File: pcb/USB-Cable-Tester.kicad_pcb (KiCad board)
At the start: 2 copper layers, 50 x 64 mm, 45 parts, among them J1 USB_C_IN, J2 USB_C_OUT, J3 USB_C_Power

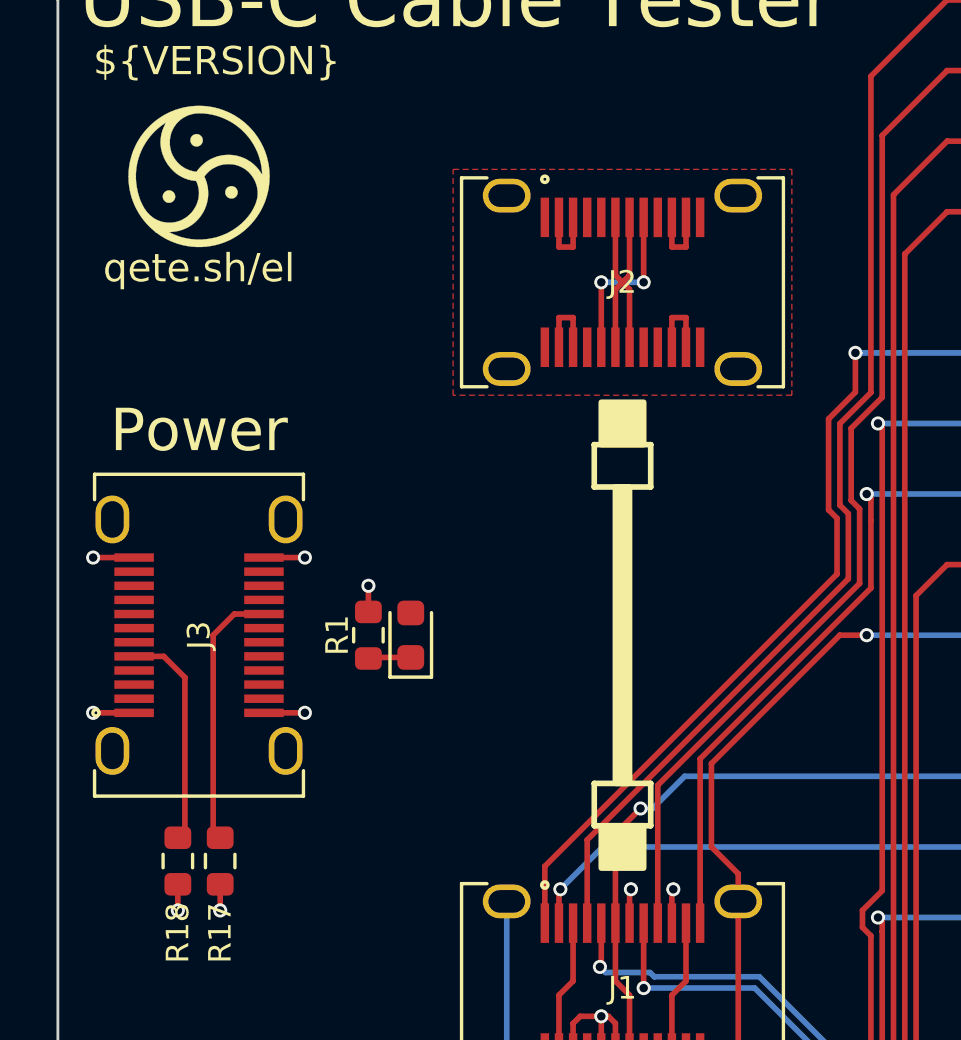
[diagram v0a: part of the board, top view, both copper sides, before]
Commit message: style: silkscreen additions
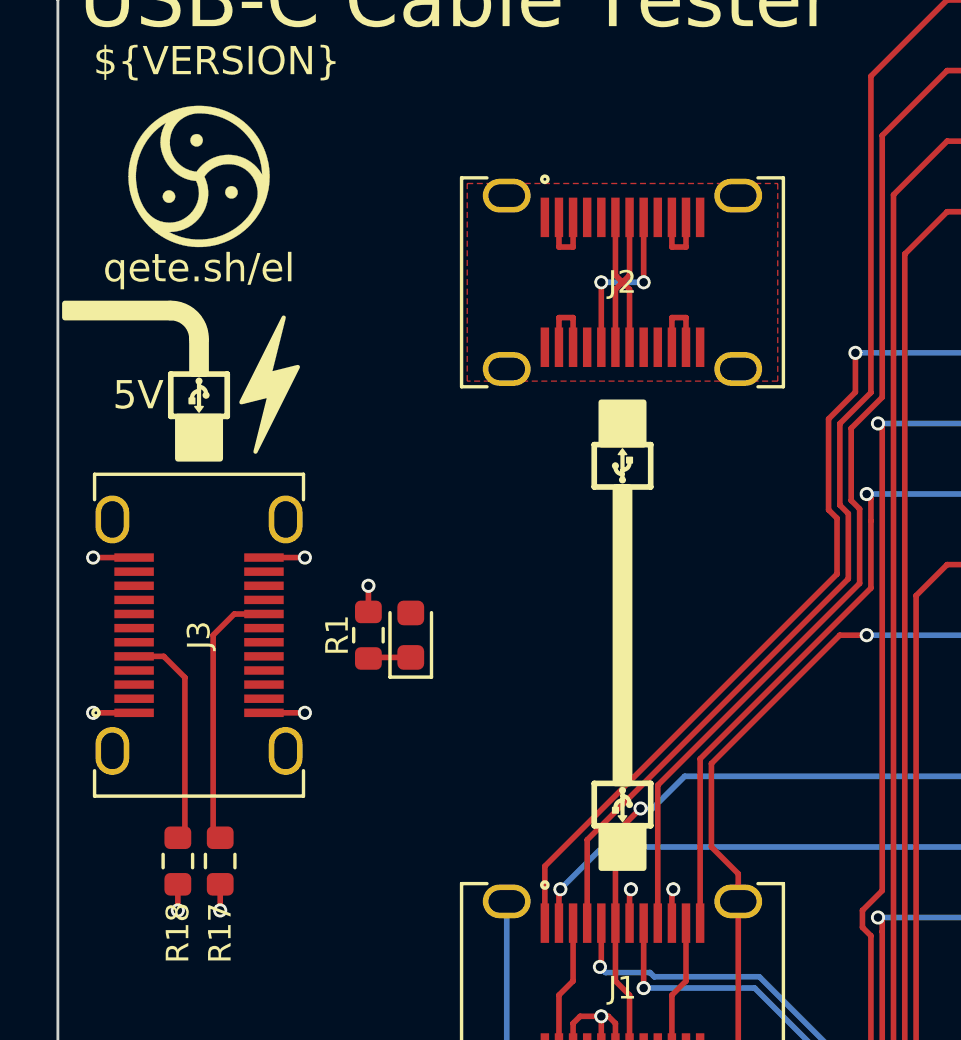
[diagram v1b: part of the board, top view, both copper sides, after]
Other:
- board text added: "5V"
- board text removed: "Power"
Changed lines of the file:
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@@
   (gr_rect (start 160.5 121.25) (end 172.5 123.75)
     (stroke (width 0.15) (type default)) (fill none) (layer "F.SilkS"))
+  (gr_circle (center 144.75 94) (end 144.85 94)
+    (stroke (width 0.05) (type solid)) (fill solid) (layer "F.SilkS"))
   (gr_rect (start 160.5 113.75) (end 172.5 118.75)
     (stroke (width 0.15) (type default)) (fill none) (layer "F.SilkS"))
+  (gr_poly
+    (pts
+      (xy 145.15 93.7)
+      (xy 145.15 93.9)
+      (xy 145.35 93.9)
+      (xy 145.35 93.7)
+    )
+    (stroke (width 0.05) (type solid)) (fill solid) (layer "F.SilkS"))
+  (gr_circle (center 130.25 91.5) (end 130.15 91.5)
+    (stroke (width 0.05) (type solid)) (fill solid) (layer "F.SilkS"))
   (gr_line (start 169 107.75) (end 169 107.5)
     (stroke (width 0.15) (type default)) (layer "F.SilkS"))
+  (gr_arc (start 145 94.3) (mid 144.823223 94.226777) (end 144.75 94.05)
+    (stroke (width 0.15) (type default)) (layer "F.SilkS"))
+  (gr_rect (start 131 92.25) (end 129 90.75)
+    (stroke (width 0.2) (type solid)) (fill none) (layer "F.SilkS"))
   (gr_line (start 160.5 98.75) (end 172.5 98.75)
     (stroke (width 0.15) (type default)) (layer "F.SilkS"))
-  (gr_rect (start 145.75 108.25) (end 144.25 106.75)
+  (gr_poly
+    (pts
+      (xy 145 93.4)
+      (xy 144.85 93.6)
+      (xy 145.15 93.6)
+    )
+    (stroke (width 0.05) (type solid)) (fill solid) (layer "F.SilkS"))
+  (gr_rect (start 144.25 106.75) (end 145.75 108.25)
     (stroke (width 0.2) (type solid)) (fill solid) (layer "F.SilkS"))
   (gr_rect (start 144.75 94.75) (end 145.25 105.25)
     (stroke (width 0.2) (type solid)) (fill solid) (layer "F.SilkS"))
+  (gr_rect (start 129.75 89.5) (end 130.25 90.75)
+    (stroke (width 0.2) (type solid)) (fill solid) (layer "F.SilkS"))
+  (gr_arc (start 129 88.5) (mid 129.707106 88.792893) (end 130 89.5)
+    (stroke (width 0.7) (type solid)) (layer "F.SilkS"))
+  (gr_poly
+    (pts
+      (xy 133 88.75)
+      (xy 131.5 91.75)
+      (xy 132.5 91.5)
+      (xy 132 93.5)
+      (xy 133.5 90.5)
+      (xy 132.5 90.75)
+    )
+    (stroke (width 0.15) (type solid)) (fill solid) (layer "F.SilkS"))
+  (gr_circle (center 145 94.5) (end 145.1 94.5)
+    (stroke (width 0.05) (type solid)) (fill solid) (layer "F.SilkS"))
+  (gr_line (start 145 94.5) (end 145 93.5)
+    (stroke (width 0.15) (type default)) (layer "F.SilkS"))
   (gr_rect (start 160.5 103.75) (end 172.5 111.25)
     (stroke (width 0.15) (type default)) (fill none) (layer "F.SilkS"))
   (gr_rect (start 144.25 91.75) (end 145.75 93.25)
     (stroke (width 0.2) (type solid)) (fill solid) (layer "F.SilkS"))
-  (gr_rect (start 146 106.75) (end 144 105.25)
+  (gr_poly
+    (pts
+      (xy 129.85 91.8)
+      (xy 129.85 91.6)
+      (xy 129.65 91.6)
+      (xy 129.65 91.8)
+    )
+    (stroke (width 0.05) (type solid)) (fill solid) (layer "F.SilkS"))
+  (gr_rect (start 125.25 88.25) (end 129 88.75)
+    (stroke (width 0.2) (type solid)) (fill solid) (layer "F.SilkS"))
+  (gr_rect (start 144 105.25) (end 146 106.75)
     (stroke (width 0.2) (type solid)) (fill none) (layer "F.SilkS"))
+  (gr_circle (center 145 105.5) (end 144.9 105.5)
+    (stroke (width 0.05) (type solid)) (fill solid) (layer "F.SilkS"))
   (gr_rect (start 160.5 88.75) (end 172.5 101.25)
     (stroke (width 0.15) (type default)) (fill none) (layer "F.SilkS"))
+  (gr_arc (start 130 91.2) (mid 130.176777 91.273223) (end 130.25 91.45)
+    (stroke (width 0.15) (type default)) (layer "F.SilkS"))
   (gr_rect (start 160.5 76.25) (end 172.5 86.25)
     (stroke (width 0.15) (type default)) (fill none) (layer "F.SilkS"))
+  (gr_arc (start 129.75 91.6) (mid 129.823223 91.423223) (end 130 91.35)
+    (stroke (width 0.15) (type default)) (layer "F.SilkS"))
+  (gr_arc (start 145.25 93.9) (mid 145.176777 94.076777) (end 145 94.15)
+    (stroke (width 0.15) (type default)) (layer "F.SilkS"))
+  (gr_poly
+    (pts
+      (xy 144.85 106.3)
+      (xy 144.85 106.1)
+      (xy 144.65 106.1)
+      (xy 144.65 106.3)
+    )
+    (stroke (width 0.05) (type solid)) (fill solid) (layer "F.SilkS"))
+  (gr_line (start 145 105.5) (end 145 106.5)
+    (stroke (width 0.15) (type default)) (layer "F.SilkS"))
+  (gr_circle (center 145.25 106) (end 145.15 106)
+    (stroke (width 0.05) (type solid)) (fill solid) (layer "F.SilkS"))
+  (gr_poly
+    (pts
+      (xy 130 92.1)
+      (xy 130.15 91.9)
+      (xy 129.85 91.9)
+    )
+    (stroke (width 0.05) (type solid)) (fill solid) (layer "F.SilkS"))
+  (gr_arc (start 145 105.7) (mid 145.176777 105.773223) (end 145.25 105.95)
+    (stroke (width 0.15) (type default)) (layer "F.SilkS"))
+  (gr_rect (start 130.75 93.75) (end 129.25 92.25)
+    (stroke (width 0.2) (type solid)) (fill solid) (layer "F.SilkS"))
   (gr_rect (start 144 93.25) (end 146 94.75)
     (stroke (width 0.2) (type solid)) (fill none) (layer "F.SilkS"))
+  (gr_arc (start 144.75 106.1) (mid 144.823223 105.923223) (end 145 105.85)
+    (stroke (width 0.15) (type default)) (layer "F.SilkS"))
+  (gr_line (start 130 91) (end 130 92)
+    (stroke (width 0.15) (type default)) (layer "F.SilkS"))
+  (gr_circle (center 130 91) (end 129.9 91)
+    (stroke (width 0.05) (type solid)) (fill solid) (layer "F.SilkS"))
+  (gr_poly
+    (pts
+      (xy 145 106.6)
+      (xy 145.15 106.4)
+      (xy 144.85 106.4)
+    )
+    (stroke (width 0.05) (type solid)) (fill solid) (layer "F.SilkS"))
   (gr_line (start 169 110) (end 167.5 110)
     (stroke (width 0.15) (type default)) (layer "F.SilkS"))
@@
     (effects (font (size 1.3 1.3) (thickness 0.15)) (justify left))
   )
-  (gr_text "Power" (at 130 92.75) (layer "F.SilkS")
-    (effects (font (size 1.5 1.5) (thickness 0.2)))
-  )
   (gr_text "4" (at 164 85) (layer "F.SilkS")
     (effects (font (size 1.3 1.3) (thickness 0.15)) (justify left))
@@
   (gr_text "4" (at 164 97.5) (layer "F.SilkS")
     (effects (font (size 1.3 1.3) (thickness 0.15)) (justify left))
+  )
+  (gr_text "5V" (at 128.75 91.5) (layer "F.SilkS")
+    (effects (font (size 1 1) (thickness 0.15)) (justify right))
   )
   (gr_text "2" (at 164 92.5) (layer "F.SilkS")
@@
     (polygon
       (pts
-        (xy 139 83.5)
-        (xy 151 83.5)
-        (xy 151 91.5)
-        (xy 139 91.5)
+        (xy 139.5 84)
+        (xy 150.5 84)
+        (xy 150.5 91)
+        (xy 139.5 91)
       )
     )
@@
     )
   )
+  (group "" (id 5d32c31c-8aa5-46ce-803e-412e4e9677af)
+    (members
+      10f09a0e-0a46-4866-8c20-ae45f77b0d39
+      1715a52b-bace-44e6-900b-5762bf8082b8
+      1cd5151f-8846-42e8-afd0-f092a6d76a02
+      357ca70e-ac7a-45ba-8f13-cf3efb9f9f7e
+      5d30872f-502f-4b05-af41-2d27e9c0246a
+      63a4bd5a-e5de-4cb0-b866-d4dec625391a
+      ae4fd08d-b8c5-4a3a-a1d6-af64db4d6b55
+    )
+  )
+  (group "" (id 65ce30b9-401a-4a4e-89ff-421d293f4610)
+    (members
+      99d2066a-1aae-45c1-ac62-6805e1d05f89
+      b6166d21-5594-4881-b8b8-359aa32cda64
+      b7b98ce6-8af4-46e5-8b95-7f0cea10d270
+      ba18b547-1d78-40ec-90db-1774d8d470c9
+      c555de68-e755-4a17-8a41-8334c8f5b5f5
+      d37ba4cf-bb8f-4a70-9922-386c20b6a82d
+      dde91862-98a9-48d7-bbcb-77b034acb908
+    )
+  )
+  (group "" (id c768af34-c85a-4a64-876b-ee73ca4ce5fc)
+    (members
+      1ae970a9-6129-4814-870e-af8eb5174833
+      78b87f14-072a-4e60-b26d-f87e52721c0f
+      a438c8b8-b479-4ae8-81ab-5f91b848c936
+      accf5bbf-427e-4879-a53e-4d45e2ba68e9
+      c3ddf47c-ad2a-4049-841e-f35863830a3f
+      d63e9578-32df-487e-9444-d8e4e2c85d26
+      d69b79cb-81d0-47ef-9ad8-e6a802ae9bd7
+    )
+  )
